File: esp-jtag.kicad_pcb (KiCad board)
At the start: 2 copper layers, 57.2 x 35.6 mm, 70 parts, among them J1 USB_B_Micro, J2 JTAG, Q1 WST03P06, Q2 S8050, Q3 S8050, SW1 SW_SPST, SW2 SW_SPST, U1 74AHC1GU04, U2 SN74AHC125RGY, U3 AMS1117-3.3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

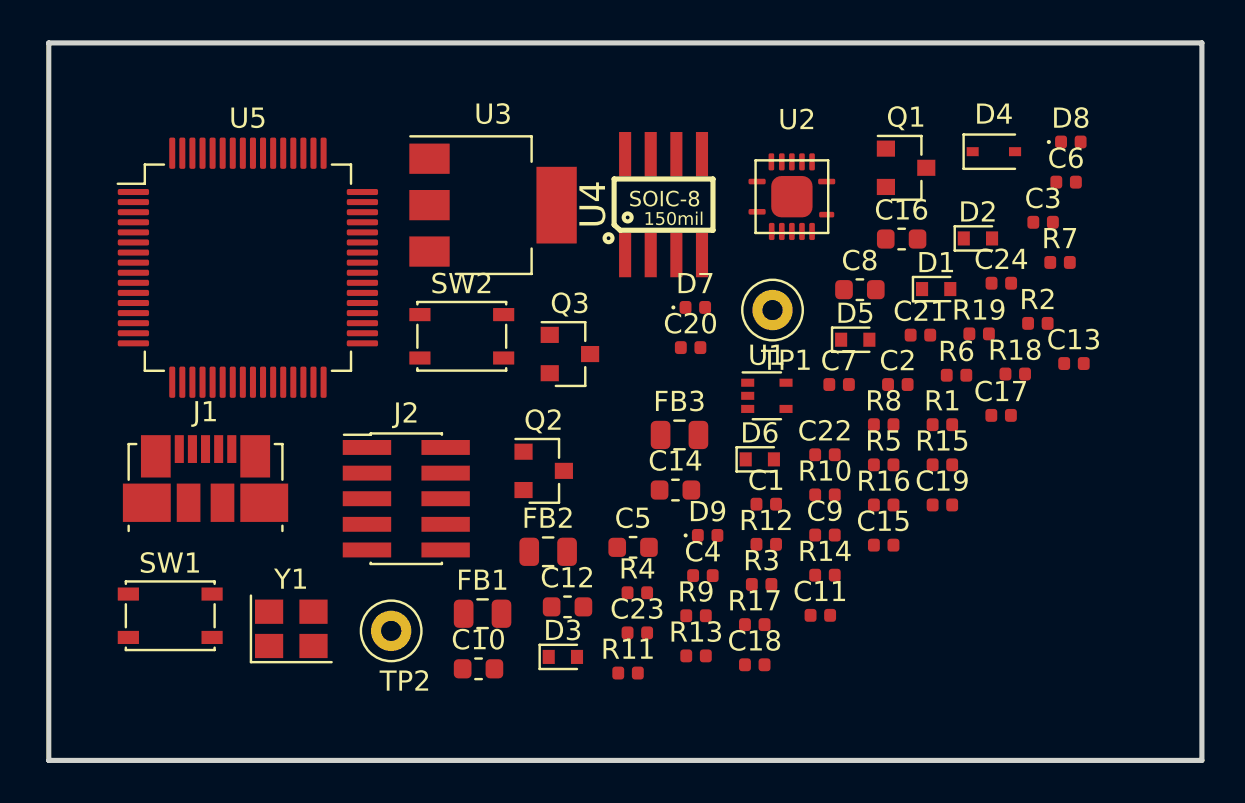
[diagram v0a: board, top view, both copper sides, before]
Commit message: Layout and route the PCB
Prepare the PCB layout by arranging the components
Route all traces and rectify mistakes in the connections
Add ground pours on top and bottom copper
Update the preview images and the README file
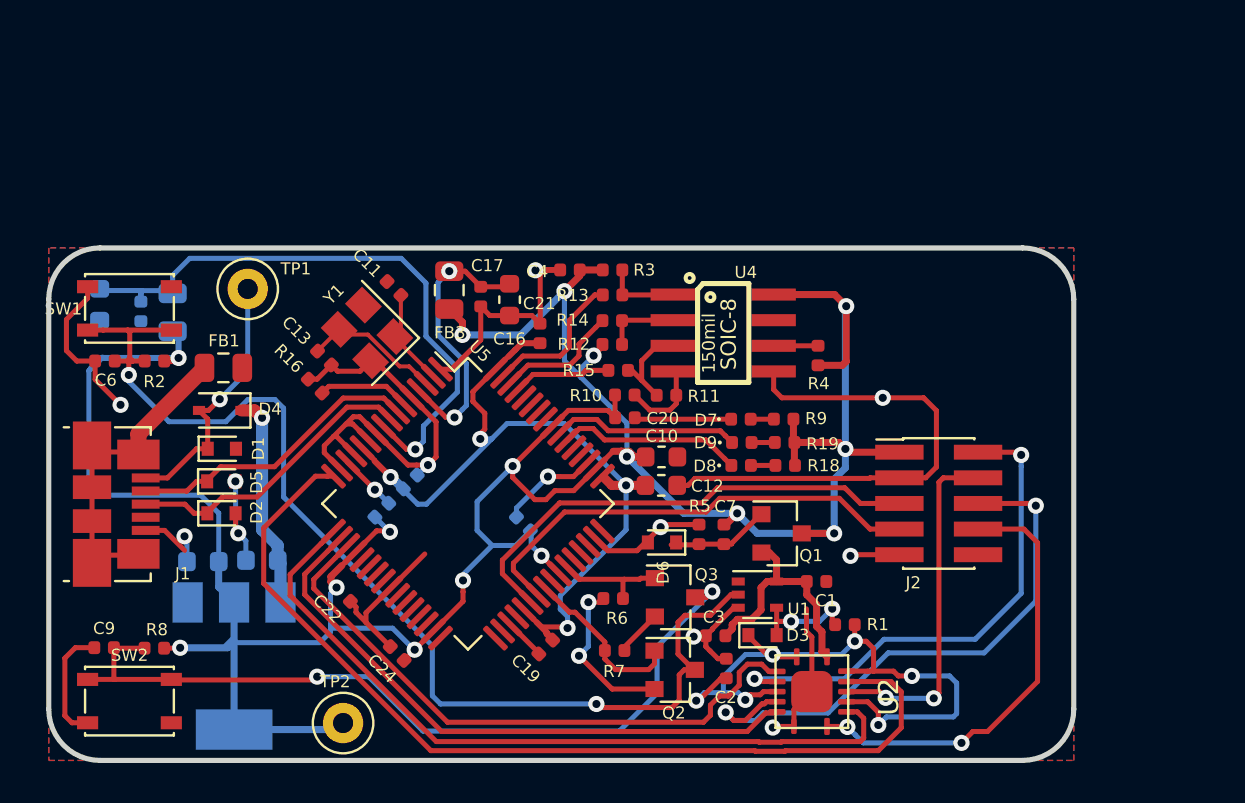
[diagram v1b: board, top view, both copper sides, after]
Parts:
- C14, C15, C18, C23, C5, C8, FB2, R17, U3: moved to B.Cu
- moved C6 48.5 mm to (193.3, 135.1), turned to 180 degrees
- moved R2 43.8 mm to (195.7, 135.1), turned to 180 degrees
- moved D4 40.4 mm to (199.0, 137.6), turned to 180 degrees
- moved D2 39.9 mm to (199.1, 142.7)
- moved C15 38.6 mm to (195.1, 132.7), turned to 270 degrees
- moved R8 37.8 mm to (195.7, 149.4), turned to 180 degrees
- moved C13 37.1 mm to (204.2, 135.0), turned to 315 degrees
- moved D1 36.3 mm to (199.1, 139.5)
- moved C9 36.2 mm to (193.2, 149.4), turned to 180 degrees
- moved C8 35.2 mm to (198.1, 145.1), turned to 180 degrees
- moved C24 35.1 mm to (207.8, 149.6), turned to 135 degrees
- moved D5 32.2 mm to (199.0, 141.1)
- moved C14 30.0 mm to (193.0, 132.4), turned to 270 degrees
- moved R7 29.3 mm to (218.5, 149.5)
- moved R16 28.8 mm to (203.7, 136.4), turned to 135 degrees
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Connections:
- J2 pad 2: FT_TMS -> ESP_TMS
- J2 pad 4: FT_TCK -> ESP_TCK
- J2 pad 5: FT_RxD -> FT_TxD
- J2 pad 6: FT_TDO -> ESP_TDO
- J2 pad 7: FT_TxD -> FT_RxD
- J2 pad 8: FT_TDI -> ESP_TDI
- U2 pad 11: (no net) -> ESP_TCK
- U2 pad 3: (no net) -> ESP_TMS
- U2 pad 5: (no net) -> ESP_TDO
- U2 pad 8: (no net) -> ESP_TDI
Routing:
- net VDD3V3: track 0.00 -> 164.4 mm, vias 0 -> 16
- net GND: track 0.00 -> 122.3 mm, vias 0 -> 12
- net ESP_EN: track 0.00 -> 55.9 mm, vias 0 -> 2
- net FT_TCK: track 0.00 -> 47.5 mm
- net VDD1V8: track 0.00 -> 41.6 mm, vias 0 -> 4
- net ESP_IO0_B: track 0.00 -> 40.4 mm, vias 0 -> 2
- net FT_TDI: track 0.00 -> 37.6 mm
- net ESP_EN_N: track 0.00 -> 34.1 mm, vias 0 -> 6
- net Net-(C14-Pad1): track 0.00 -> 30.9 mm, vias 0 -> 1
- net FT_TMS: track 0.00 -> 30.5 mm
- net FT_TDO: track 0.00 -> 30.2 mm
- net ESP_TDO: track 0.00 -> 28.7 mm, vias 0 -> 2
- net ESP_TMS: track 0.00 -> 25.2 mm, vias 0 -> 2
- net FT_TxD: track 0.00 -> 24.2 mm
- net FT_RxD: track 0.00 -> 23.2 mm
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- added copper zone on B.Cu, net GND
- added copper zone on F.Cu, net GND
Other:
- board size 57.2 x 35.6 mm -> 50.8 x 25.4 mm
- net class 1V8 added: clearance 0.2, trace_width 0.3, via_dia 0.8, via_drill 0.4
- net class 3V3 added: clearance 0.2, trace_width 0.3, via_dia 0.8, via_drill 0.4
- net class 5V added: clearance 0.25, trace_width 0.6, via_dia 1, via_drill 0.6
- net class crystal added: clearance 0.1, trace_width 0.2, via_dia 0.8, via_drill 0.4

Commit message: Minor tweaks
Finalize PCB layout, especially top silkscreen
Export ray-tracing renders
Update the README file
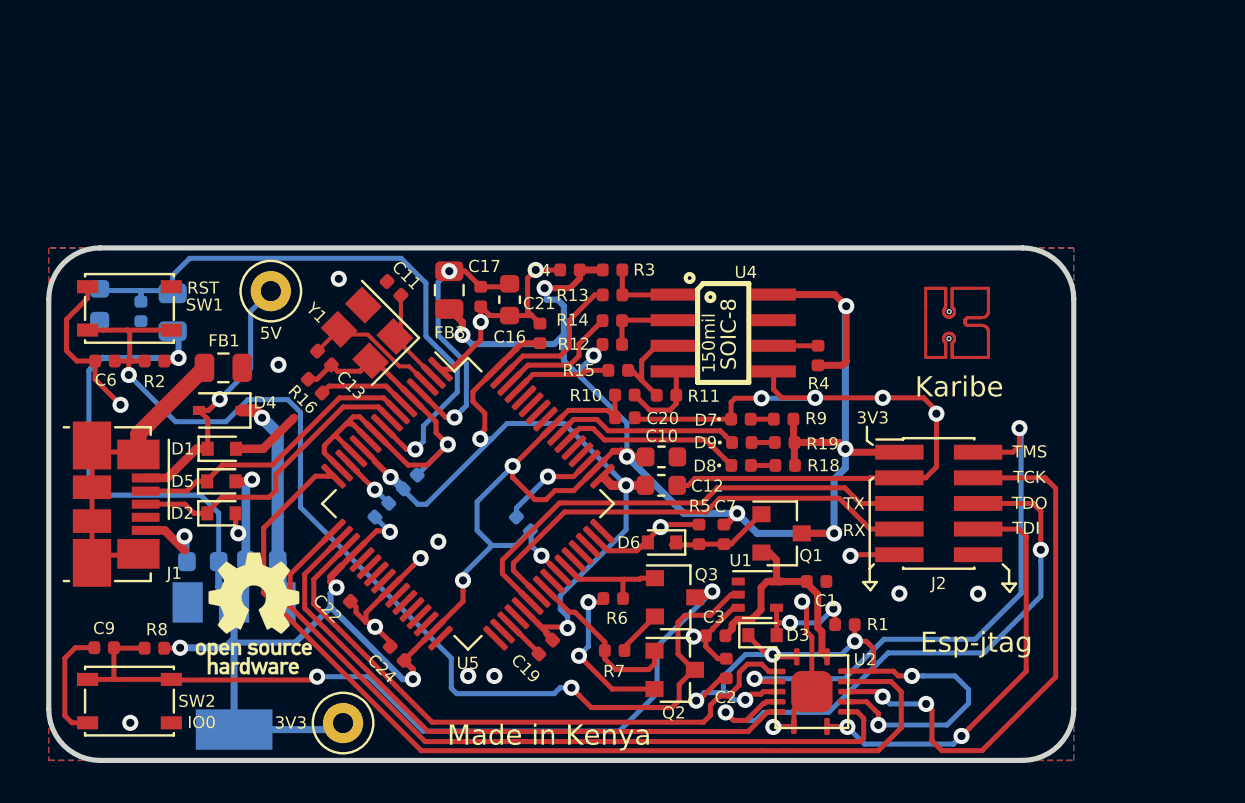
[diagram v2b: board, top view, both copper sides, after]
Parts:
- added L1: karibe_logo, artwork:karibe_logo, F.Cu at (235.1, 133.3)
- added REF**: OSHW-Logo_5.7x6mm_SilkScreen, Symbol:OSHW-Logo_5.7x6mm_SilkScreen, F.Cu at (200.7, 147.7)
- moved TP1 1.15 mm to (201.5, 131.7)
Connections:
- J2 pad 10: (no net) -> GND
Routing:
- net GND: track 122.3 -> 133.2 mm, vias 12 -> 27
- net ESP_TCK: track 17.3 -> 27.4 mm
- net VDD3V3: track 164.4 -> 167.1 mm
- net ESP_TMS: track 25.2 -> 27.4 mm
- net ESP_TDI: track 22.1 -> 20.9 mm
- net ESP_EN: track 55.9 -> 55.2 mm
- net ESP_EN_N: track 34.1 -> 34.8 mm
- net USB_DP: track 14.8 -> 15.3 mm
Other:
- board text added: "3V3"
- board text added: "5V"
- board text added: "Esp-jtag"
- board text added: "IO0"
- board text added: "Karibe"
- board text added: "Made in Kenya"
- board text added: "RST"
- board text added: "RX"
- board text added: "TCK"
- board text added: "TDI"
- board text added: "TDO"
- board text added: "TMS"
- board text added: "TX"
